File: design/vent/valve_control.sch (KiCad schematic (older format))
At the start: 15 parts, among them J11 Conn_01x02, J12 Conn_01x03, J13 Conn_01x03, Q3 Q_PMOS_GSD, Q4 Q_PMOS_GSD, Q5 Q_NPN_BEC, Q6 Q_NMOS_GSD, Q7 Q_NMOS_GSD, Q8 Q_NPN_BEC

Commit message: Refine schematic
- Add part numbers and correct pinout for mosfets
- Add fuses to battery inputs
- Add decoupling caps to logic translators
- Add flyback diodes to H Bridge, to be populated if the body diodes of
  the mosfets are not sufficient.
- Change H Bridge to operate with 4 inputs instead of 2.

Also, misc directory cleanup.
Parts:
- removed Q3, Q4: Q_PMOS_GSD, symbol Q_PMOS_GSD
- removed Q5, Q8: Q_NPN_BEC, symbol Q_NPN_BEC
- removed Q7: Q_NMOS_GSD, symbol Q_NMOS_GSD
- added D1, D2, D3, D4: D, symbol D
- added F2: Fuse_Small, symbol Fuse_Small
- added Q3, Q4: AOD417, symbol Q_PMOS_GDS
- added Q5: DMG2302UK, symbol Q_NMOS_GSD
- added Q7, Q8: AOD476, symbol Q_NMOS_GDS
- added R12, R13: 10K, symbol R
- Q6: value Q_NMOS_GSD -> DMG2302UK
- R10, R11: value R -> 10K
- renumbered J11 to J13, J12 to J14, J13 to J15
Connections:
- net labels added: HIGH_SIDE_A, HIGH_SIDE_B, LOW_SIDE_A, LOW_SIDE_B
- net labels removed: INPUT_A, INPUT_B
- wire segments 50 -> 52
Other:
- note added: "D1-D4 to be populated only if the mosfet\nbody diodes aren't sufficient as flyback diodes."
- note removed: "TODO: pullups for default state"
- moved on the sheet: J13, R8, R9

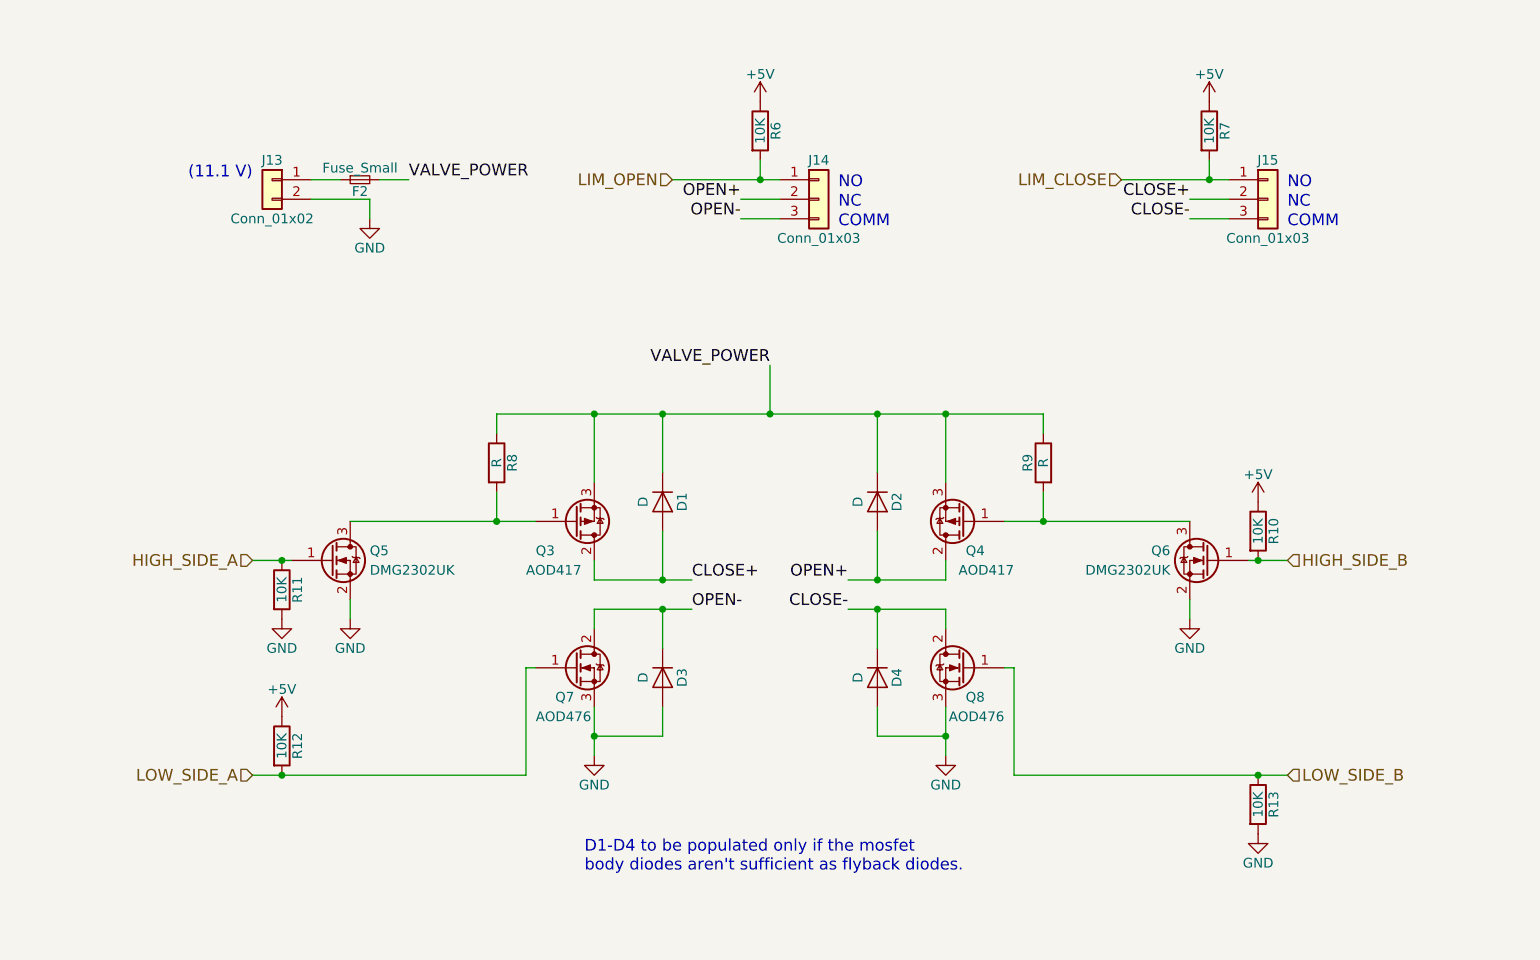
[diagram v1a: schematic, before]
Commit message: Review changes
- Add debug LEDs
- Add pullup resistors on logic shifters for xbee and sd card.
- Add 0 ohm resistor between valve and control power sources (to allow
  for either one of both sources to be used).
- Add another IMU
- Add gate resistors to valve control mosfets
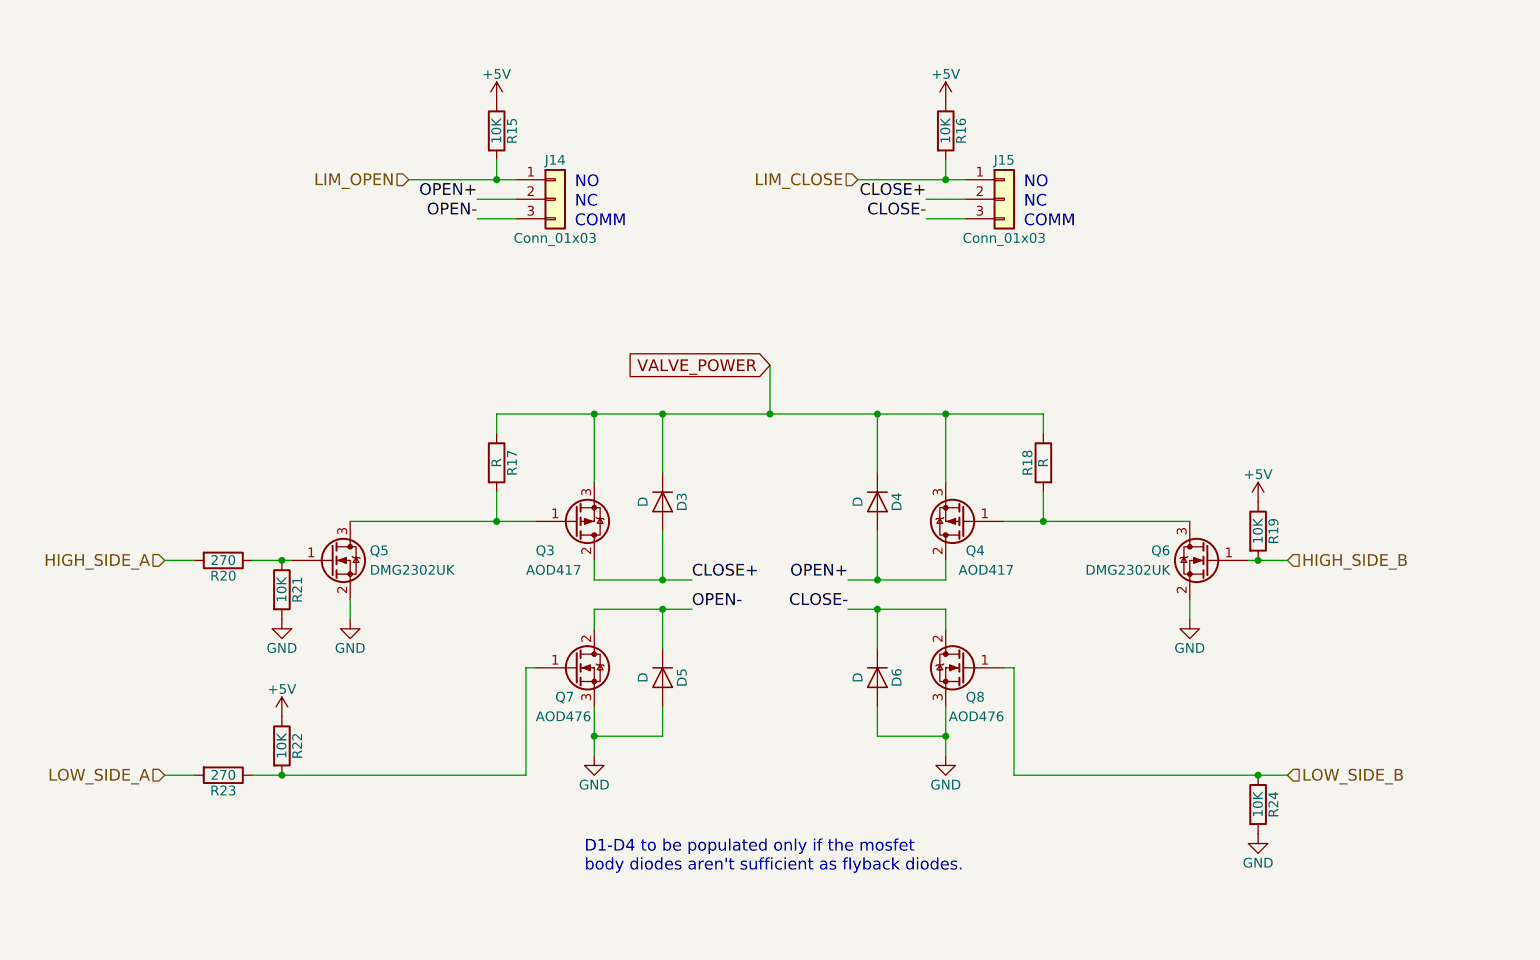
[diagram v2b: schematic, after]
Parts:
- removed F2: Fuse_Small, symbol Fuse_Small
- removed J13: Conn_01x02, symbol Conn_01x02
- added R20, R23: 270, symbol R
- renumbered D1 to D3, D2 to D4, D3 to D5, D4 to D6, R6 to R15, R7 to R16, R8 to R17, R9 to R18, R10 to R19, R11 to R21, R12 to R22, R13 to R24
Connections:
- net HIGH_SIDE_A: now also R20.2; no longer Q5.1 (G), R21.1
- net LOW_SIDE_A: now also R23.2; no longer Q7.1 (G), R22.2
- new net: Q5.1 (G), R20.1, R21.1
- new net: Q7.1 (G), R22.2, R23.1
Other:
- note removed: "(11.1 V)"
- moved on the sheet: J14, J15, R15, R16

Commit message: Fix MOSFET gate resistors
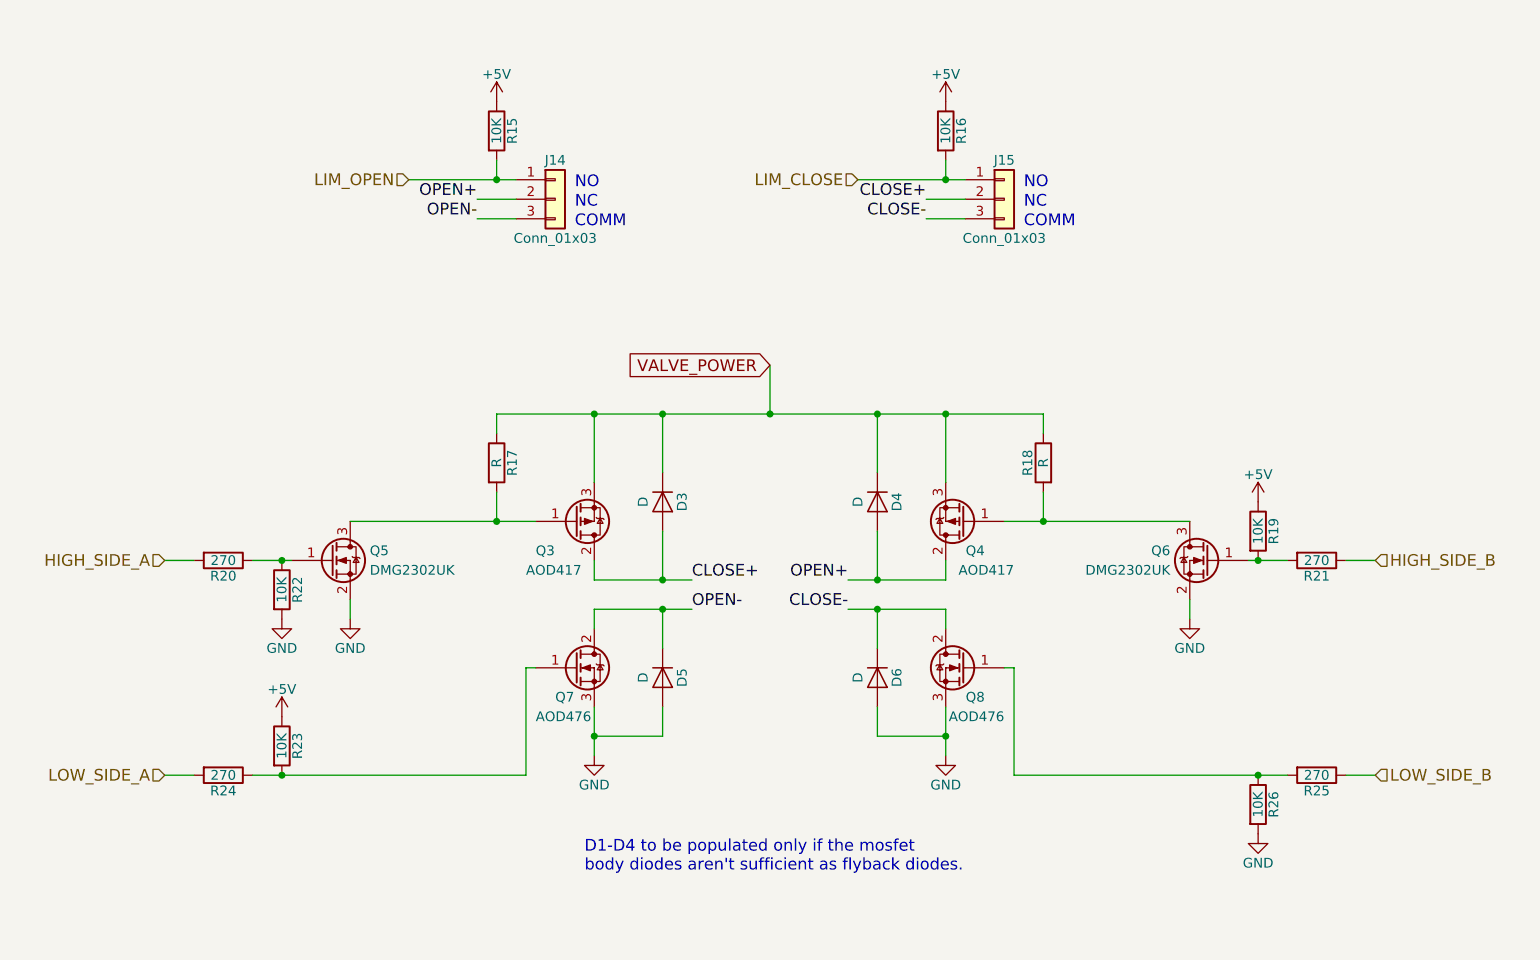
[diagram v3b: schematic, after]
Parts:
- added R21, R25: 270, symbol R
- renumbered R21 to R22, R22 to R23, R23 to R24, R24 to R26
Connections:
- net HIGH_SIDE_B: now also R21.1; no longer Q6.1 (G), R19.2
- net LOW_SIDE_B: now also R25.1; no longer Q8.1 (G), R26.1
- new net: Q8.1 (G), R25.2, R26.1
- new net: Q6.1 (G), R19.2, R21.2
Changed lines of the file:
@@
 $EndComp
 $Comp
-L R R21
+L R R22
 U 1 1 5AEA8243
 P 3100 4350
-F 0 "R21" V 3180 4350 50  0000 C CNN
+F 0 "R22" V 3180 4350 50  0000 C CNN
 F 1 "10K" V 3100 4350 50  0000 C CNN
 F 2 "" V 3030 4350 50  0001 C CNN
@@
 LOW_SIDE_A
 $Comp
-L R R22
+L R R23
 U 1 1 5AEBEFF0
 P 3100 5150
-F 0 "R22" V 3180 5150 50  0000 C CNN
+F 0 "R23" V 3180 5150 50  0000 C CNN
 F 1 "10K" V 3100 5150 50  0000 C CNN
 F 2 "" V 3030 5150 50  0001 C CNN
@@
 	-1   0    0    -1
 $EndComp
-Text HLabel 8250 4200 2    60   Input ~ 0
+Text HLabel 8700 4200 2    60   Input ~ 0
 HIGH_SIDE_B
 $Comp
@@
 	-1   0    0    -1
 $EndComp
-Text HLabel 8250 5300 2    60   Input ~ 0
+Text HLabel 8700 5300 2    60   Input ~ 0
 LOW_SIDE_B
 $Comp
@@
 $EndComp
 Wire Wire Line
-	4700 4950 4700 5100
-Wire Wire Line
-	4700 5100 4700 5200
-Wire Wire Line
-	6500 4950 6500 5100
-Wire Wire Line
-	6500 5100 6500 5200
-Wire Wire Line
-	4700 4300 5050 4300
-Wire Wire Line
-	5050 4300 5200 4300
+	4700 4950 4700 5200
+Wire Wire Line
+	6500 4950 6500 5200
+Wire Wire Line
+	4700 4300 5200 4300
 Wire Wire Line
 	4700 4300 4700 4200
 Wire Wire Line
-	6000 4300 6150 4300
-Wire Wire Line
-	6150 4300 6500 4300
+	6000 4300 6500 4300
 Wire Wire Line
 	6500 4300 6500 4200
 Wire Wire Line
-	6000 4450 6150 4450
-Wire Wire Line
-	6150 4450 6500 4450
+	6000 4450 6500 4450
 Wire Wire Line
 	6500 4450 6500 4550
 Wire Wire Line
-	4700 4450 5050 4450
-Wire Wire Line
-	5050 4450 5200 4450
+	4700 4450 5200 4450
 Wire Wire Line
 	4700 4450 4700 4550
 Wire Wire Line
-	4200 3450 4700 3450
-Wire Wire Line
-	4700 3450 5050 3450
-Wire Wire Line
-	5050 3450 5600 3450
-Wire Wire Line
-	5600 3450 6150 3450
-Wire Wire Line
-	6150 3450 6500 3450
-Wire Wire Line
-	6500 3450 7000 3450
+	4200 3450 7000 3450
 Wire Wire Line
 	4700 3450 4700 3800
@@
 	6500 3450 6500 3800
 Wire Wire Line
-	3450 4000 4200 4000
-Wire Wire Line
-	4200 4000 4400 4000
+	3450 4000 4400 4000
 Wire Wire Line
 	4200 3550 4200 3450
@@
 	3450 4500 3450 4400
 Wire Wire Line
-	6800 4000 7000 4000
-Wire Wire Line
-	7000 4000 7750 4000
+	6800 4000 7750 4000
 Wire Wire Line
 	7000 3450 7000 3550
@@
 Connection ~ 6500 3450
 Wire Wire Line
-	2950 4200 3100 4200
-Wire Wire Line
-	3100 4200 3150 4200
+	2950 4200 3150 4200
 Wire Wire Line
 	4100 2450 4300 2450
@@
 	4100 2350 4300 2350
 Wire Wire Line
-	3750 2250 4200 2250
-Wire Wire Line
-	4200 2250 4300 2250
+	3750 2250 4300 2250
 Wire Wire Line
 	4200 2150 4200 2250
@@
 	6400 2350 6600 2350
 Wire Wire Line
-	6050 2250 6500 2250
-Wire Wire Line
-	6500 2250 6600 2250
+	6050 2250 6600 2250
 Wire Wire Line
 	6500 2150 6500 2250
@@
 	4200 3850 4200 4000
 Wire Wire Line
-	2950 5300 3100 5300
-Wire Wire Line
-	3100 5300 4350 5300
+	2950 5300 4350 5300
 Wire Wire Line
 	4400 4750 4350 4750
@@
 	7750 4500 7750 4400
 Wire Wire Line
-	8050 4200 8100 4200
-Wire Wire Line
-	8100 4200 8250 4200
-Wire Wire Line
-	6850 5300 8100 5300
-Wire Wire Line
-	8100 5300 8250 5300
+	8050 4200 8250 4200
+Wire Wire Line
+	6850 5300 8250 5300
 Wire Wire Line
 	6800 4750 6850 4750
@@
 Connection ~ 8100 4200
 $Comp
-L R R24
+L R R26
 U 1 1 5AEC1285
 P 8100 5450
-F 0 "R24" V 8180 5450 50  0000 C CNN
+F 0 "R26" V 8180 5450 50  0000 C CNN
 F 1 "10K" V 8100 5450 50  0000 C CNN
 F 2 "" V 8030 5450 50  0001 C CNN
@@
 	2650 4200 2500 4200
 $Comp
-L R R23
+L R R24
 U 1 1 5AEFDDA3
 P 2800 5300
-F 0 "R23" V 2880 5300 50  0000 C CNN
+F 0 "R24" V 2880 5300 50  0000 C CNN
 F 1 "270" V 2800 5300 50  0000 C CNN
 F 2 "" V 2730 5300 50  0001 C CNN
@@
 VALVE_POWER
 Connection ~ 3100 5300
+$Comp
+L R R21
+U 1 1 5AF0484A
+P 8400 4200
+F 0 "R21" V 8480 4200 50  0000 C CNN
+F 1 "270" V 8400 4200 50  0000 C CNN
+F 2 "" V 8330 4200 50  0001 C CNN
+F 3 "" H 8400 4200 50  0001 C CNN
+	1    8400 4200
+	0    1    1    0
+$EndComp
+$Comp
+L R R25
+U 1 1 5AF048C3
+P 8400 5300
+F 0 "R25" V 8480 5300 50  0000 C CNN
+F 1 "270" V 8400 5300 50  0000 C CNN
+F 2 "" V 8330 5300 50  0001 C CNN
+F 3 "" H 8400 5300 50  0001 C CNN
+	1    8400 5300
+	0    1    1    0
+$EndComp
+Wire Wire Line
+	8550 4200 8700 4200
+Wire Wire Line
+	8550 5300 8700 5300
 $EndSCHEMATC

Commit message: Add support for injector valve default state
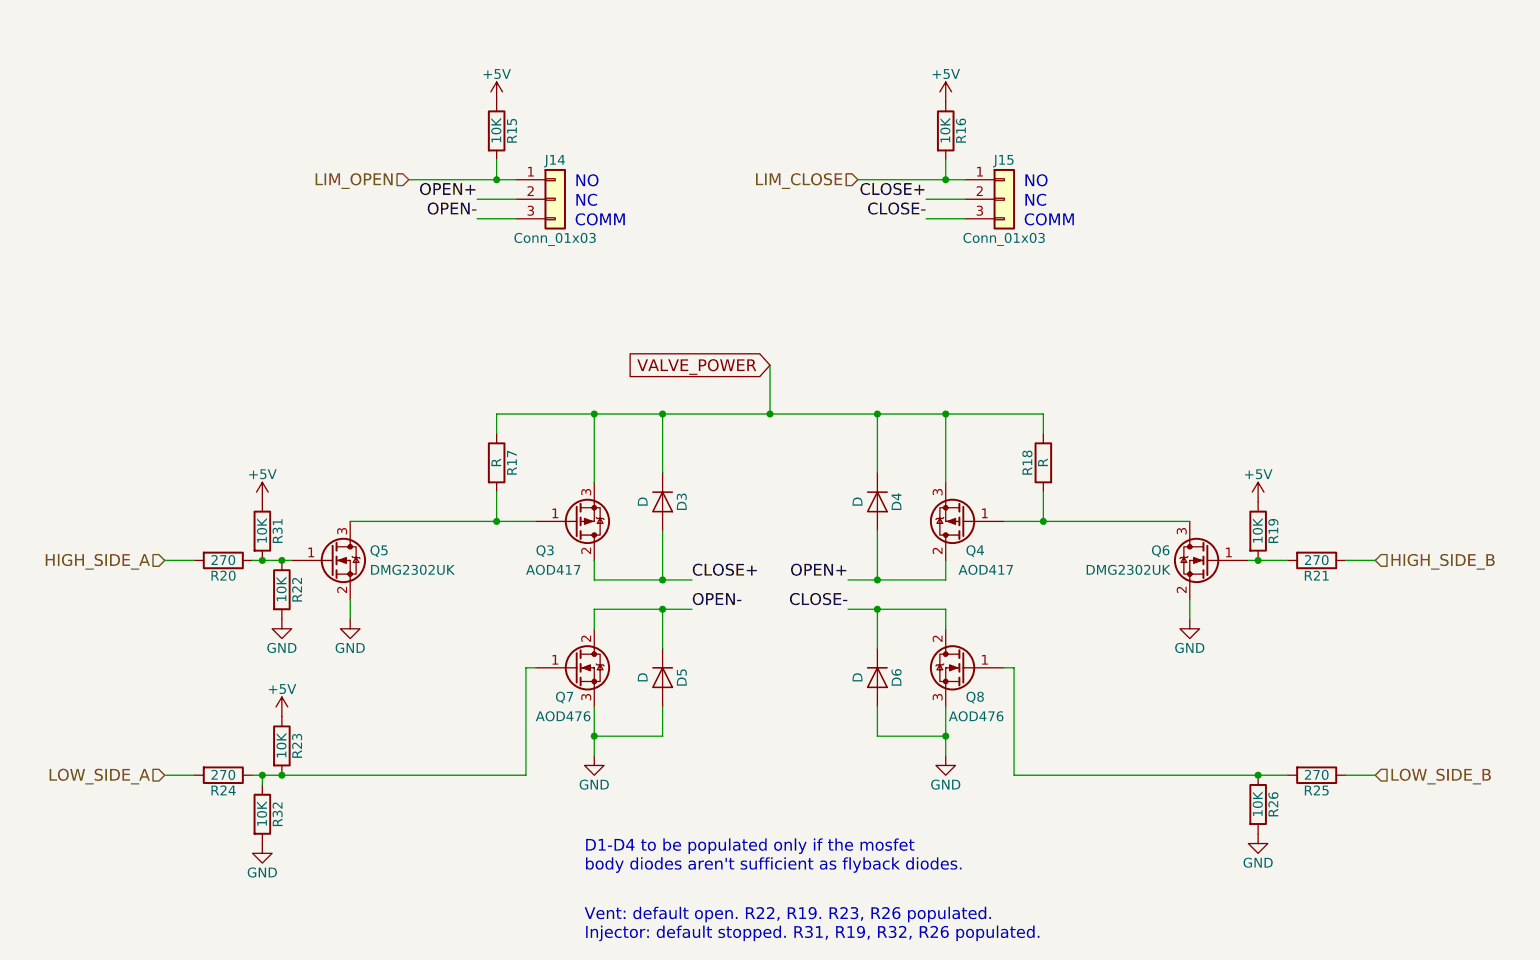
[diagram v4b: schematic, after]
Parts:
- added R31, R32: 10K, symbol R
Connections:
- net +5V: now also R31.1
- net GND: now also R32.2
- net at Q5.1 (G), R20.1, R22.1: now also R31.2
- net at Q7.1 (G), R23.2, R24.1: now also R32.1
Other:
- note added: "Vent: default open. R22, R19. R23, R26 populated.\nInjector: default stopped. R31, R19, R32, R26 populated."
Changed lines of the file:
@@
 $EndDescr
 $Comp
-L GND #PWR82
+L GND #PWR83
 U 1 1 5AE16382
 P 4700 5200
-F 0 "#PWR82" H 4700 4950 50  0001 C CNN
+F 0 "#PWR83" H 4700 4950 50  0001 C CNN
 F 1 "GND" H 4700 5050 50  0000 C CNN
 F 2 "" H 4700 5200 50  0001 C CNN
@@
 $EndComp
 $Comp
-L GND #PWR83
+L GND #PWR84
 U 1 1 5AE163E6
 P 6500 5200
-F 0 "#PWR83" H 6500 4950 50  0001 C CNN
+F 0 "#PWR84" H 6500 4950 50  0001 C CNN
 F 1 "GND" H 6500 5050 50  0000 C CNN
 F 2 "" H 6500 5200 50  0001 C CNN
@@
 $EndComp
 $Comp
-L GND #PWR79
+L GND #PWR80
 U 1 1 5AE172FE
 P 3450 4500
-F 0 "#PWR79" H 3450 4250 50  0001 C CNN
+F 0 "#PWR80" H 3450 4250 50  0001 C CNN
 F 1 "GND" H 3450 4350 50  0000 C CNN
 F 2 "" H 3450 4500 50  0001 C CNN
@@
 $EndComp
 $Comp
-L GND #PWR78
+L GND #PWR79
 U 1 1 5AEBE82B
 P 3100 4500
-F 0 "#PWR78" H 3100 4250 50  0001 C CNN
+F 0 "#PWR79" H 3100 4250 50  0001 C CNN
 F 1 "GND" H 3100 4350 50  0000 C CNN
 F 2 "" H 3100 4500 50  0001 C CNN
@@
 $EndComp
 $Comp
-L +5V #PWR81
+L +5V #PWR82
 U 1 1 5AEBF207
 P 3100 5000
-F 0 "#PWR81" H 3100 4850 50  0001 C CNN
+F 0 "#PWR82" H 3100 4850 50  0001 C CNN
 F 1 "+5V" H 3100 5140 50  0000 C CNN
 F 2 "" H 3100 5000 50  0001 C CNN
@@
 $EndComp
 $Comp
-L GND #PWR80
+L GND #PWR81
 U 1 1 5AEBFD20
 P 7750 4500
-F 0 "#PWR80" H 7750 4250 50  0001 C CNN
+F 0 "#PWR81" H 7750 4250 50  0001 C CNN
 F 1 "GND" H 7750 4350 50  0000 C CNN
 F 2 "" H 7750 4500 50  0001 C CNN
@@
 $EndComp
 $Comp
-L GND #PWR84
+L GND #PWR85
 U 1 1 5AEBFD35
 P 8100 5600
-F 0 "#PWR84" H 8100 5350 50  0001 C CNN
+F 0 "#PWR85" H 8100 5350 50  0001 C CNN
 F 1 "GND" H 8100 5450 50  0000 C CNN
 F 2 "" H 8100 5600 50  0001 C CNN
@@
 LOW_SIDE_B
 $Comp
-L +5V #PWR77
+L +5V #PWR78
 U 1 1 5AEBFD4A
 P 8100 3900
-F 0 "#PWR77" H 8100 3750 50  0001 C CNN
+F 0 "#PWR78" H 8100 3750 50  0001 C CNN
 F 1 "+5V" H 8100 4040 50  0000 C CNN
 F 2 "" H 8100 3900 50  0001 C CNN
@@
 Wire Wire Line
 	8550 5300 8700 5300
+$Comp
+L R R31
+U 1 1 5AF1068C
+P 3000 4050
+F 0 "R31" V 3080 4050 50  0000 C CNN
+F 1 "10K" V 3000 4050 50  0000 C CNN
+F 2 "" V 2930 4050 50  0001 C CNN
+F 3 "" H 3000 4050 50  0001 C CNN
+	1    3000 4050
+	1    0    0    -1
+$EndComp
+$Comp
+L +5V #PWR77
+U 1 1 5AF107D5
+P 3000 3900
+F 0 "#PWR77" H 3000 3750 50  0001 C CNN
+F 1 "+5V" H 3000 4040 50  0000 C CNN
+F 2 "" H 3000 3900 50  0001 C CNN
+F 3 "" H 3000 3900 50  0001 C CNN
+	1    3000 3900
+	1    0    0    -1
+$EndComp
+Connection ~ 3000 4200
+$Comp
+L R R32
+U 1 1 5AF10A7A
+P 3000 5500
+F 0 "R32" V 3080 5500 50  0000 C CNN
+F 1 "10K" V 3000 5500 50  0000 C CNN
+F 2 "" V 2930 5500 50  0001 C CNN
+F 3 "" H 3000 5500 50  0001 C CNN
+	1    3000 5500
+	1    0    0    -1
+$EndComp
+$Comp
+L GND #PWR86
+U 1 1 5AF10AEB
+P 3000 5650
+F 0 "#PWR86" H 3000 5400 50  0001 C CNN
+F 1 "GND" H 3000 5500 50  0000 C CNN
+F 2 "" H 3000 5650 50  0001 C CNN
+F 3 "" H 3000 5650 50  0001 C CNN
+	1    3000 5650
+	1    0    0    -1
+$EndComp
+Wire Wire Line
+	3000 5350 3000 5300
+Connection ~ 3000 5300
+Text Notes 4650 6150 0    60   ~ 0
+Vent: default open. R22, R19. R23, R26 populated.\nInjector: default stopped. R31, R19, R32, R26 populated.
 $EndSCHEMATC
